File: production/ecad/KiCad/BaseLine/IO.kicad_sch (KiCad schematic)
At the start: 6 parts, among them J10 LoadCell1, J11 LoadCell2, J12 LoadCell3, J13 LoadCell4, J14 Conn_01x04_Socket, U12 CD74HC4067M96

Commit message: fixing connectors I placed
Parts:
- removed J14: Conn_01x04_Socket, Connector_JST:JST_EH_B4B-EH-A_1x04_P2.50mm_Vertical, symbol Connector:Conn_01x04_Socket
- added J17: IMU_connector, symbol Connector:Conn_01x04_Socket
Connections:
- net +3.3V: now also J17.1 (Pin_1)
- net GND: now also J17.4 (Pin_4)
- net SCL: now also J17.2 (Pin_2)
- net SDA: now also J17.3 (Pin_3)
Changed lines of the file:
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@@
-	)
-	(symbol
-		(lib_id "Connector:Conn_01x04_Socket")
-		(at 212.09 76.2 180)
-		(unit 1)
-		(exclude_from_sim no)
-		(in_bom yes)
-		(on_board yes)
-		(dnp no)
-		(property "Reference" "J14"
-			(at 215.392 61.468 0)
-			(effects
-				(font
-					(size 1.27 1.27)
-				)
-			)
-		)
-		(property "Value" "Conn_01x04_Socket"
-			(at 212.725 68.58 0)
-			(effects
-				(font
-					(size 1.27 1.27)
-				)
-				(hide yes)
-			)
-		)
-		(property "Footprint" "Connector_JST:JST_EH_B4B-EH-A_1x04_P2.50mm_Vertical"
-			(at 212.09 76.2 0)
-			(effects
-				(font
-					(size 1.27 1.27)
-				)
-				(hide yes)
-			)
-		)
-		(property "Datasheet" "~"
-			(at 212.09 76.2 0)
-			(effects
-				(font
-					(size 1.27 1.27)
-				)
-				(hide yes)
-			)
-		)
-		(property "Description" "Generic connector, single row, 01x04, script generated"
-			(at 212.09 76.2 0)
-			(effects
-				(font
-					(size 1.27 1.27)
-				)
-				(hide yes)
-			)
-		)
-		(pin "1"
-		)
-		(pin "3"
-		)
-		(pin "4"
-		)
-		(pin "2"
-		)
-		(instances
-			(project "BaseLine"
-				(path "/ba9eda21-3882-41e1-8265-3d8ac781da20/e3080f39-1d26-4bce-b471-534f477eeea5"
-					(reference "J14")
-					(unit 1)
-				)
-			)
-		)
 	)
 	(symbol
@@
 					(unit 1)
 				)
+			)
+		)
+	)
+	(symbol
+		(lib_id "Connector:Conn_01x04_Socket")
+		(at 212.09 73.66 0)
+		(mirror y)
+		(unit 1)
+		(exclude_from_sim no)
+		(in_bom yes)
+		(on_board yes)
+		(dnp no)
+		(property "Reference" "J17"
+			(at 210.82 73.6599 0)
+			(effects
+				(font
+					(size 1.27 1.27)
+				)
+				(justify left)
+			)
+		)
+		(property "Value" "IMU_connector"
+			(at 210.82 76.1999 0)
+			(effects
+				(font
+					(size 1.27 1.27)
+				)
+				(justify left)
+			)
+		)
+		(property "Footprint" ""
+			(at 212.09 73.66 0)
+			(effects
+				(font
+					(size 1.27 1.27)
+				)
+				(hide yes)
+			)
+		)
+		(property "Datasheet" "~"
+			(at 212.09 73.66 0)
+			(effects
+				(font
+					(size 1.27 1.27)
+				)
+				(hide yes)
+			)
+		)
+		(property "Description" "Generic connector, single row, 01x04, script generated"
+			(at 212.09 73.66 0)
+			(effects
+				(font
+					(size 1.27 1.27)
+				)
+				(hide yes)
+			)
+		)
+		(pin "1"
+		)
+		(pin "3"
+		)
+		(pin "2"
+		)
+		(pin "4"
+		)
+		(instances
+			(project ""
+				(path "/ba9eda21-3882-41e1-8265-3d8ac781da20/e3080f39-1d26-4bce-b471-534f477eeea5"
+					(reference "J17")
+					(unit 1)
+				)

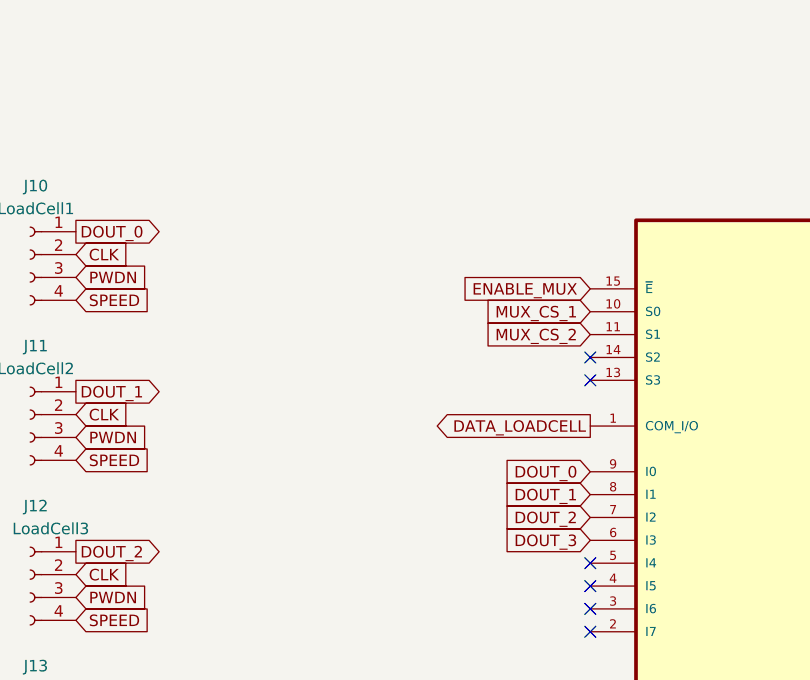
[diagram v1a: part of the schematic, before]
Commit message: fixing MUX
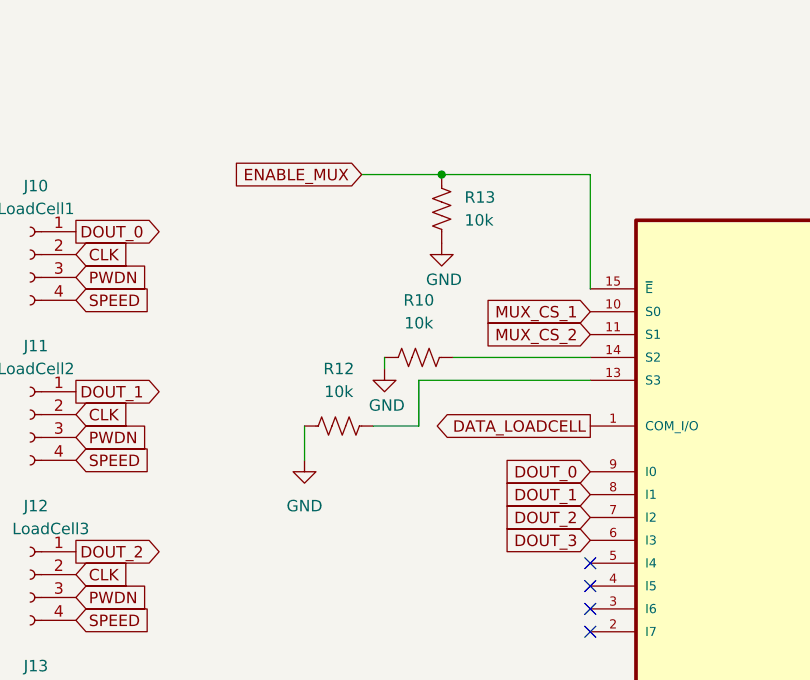
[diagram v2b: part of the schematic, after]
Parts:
- added R10, R12, R13: 10k, symbol Device:R_US
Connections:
- net ENABLE_MUX: now also R13.2
- net GND: now also R10.1, R12.1, R13.1
- net at U12.13 (S3): now also R12.2
- net at U12.14 (S2): now also R10.2
- no-connect marks 14 -> 12

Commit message: Added some footprints
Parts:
- R10, R12, R13: footprint (none) -> Resistor_SMD:R_0805_2012Metric_Pad1.20x1.40mm_HandSolder
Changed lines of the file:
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@@
 			)
 		)
-		(property "Footprint" ""
+		(property "Footprint" "Resistor_SMD:R_0805_2012Metric_Pad1.20x1.40mm_HandSolder"
 			(at 99.314 98.044 90)
 			(effects
@@
 			)
 		)
-		(property "Footprint" ""
+		(property "Footprint" "Resistor_SMD:R_0805_2012Metric_Pad1.20x1.40mm_HandSolder"
 			(at 109.474 74.676 90)
 			(effects
@@
 			)
 		)
-		(property "Footprint" ""
+		(property "Footprint" "Resistor_SMD:R_0805_2012Metric_Pad1.20x1.40mm_HandSolder"
 			(at 108.204 90.424 90)
 			(effects
